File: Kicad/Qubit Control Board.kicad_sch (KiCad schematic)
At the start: 2 parts, among them U1 TRF372017IRGZR, U2 AD9743BCPZ

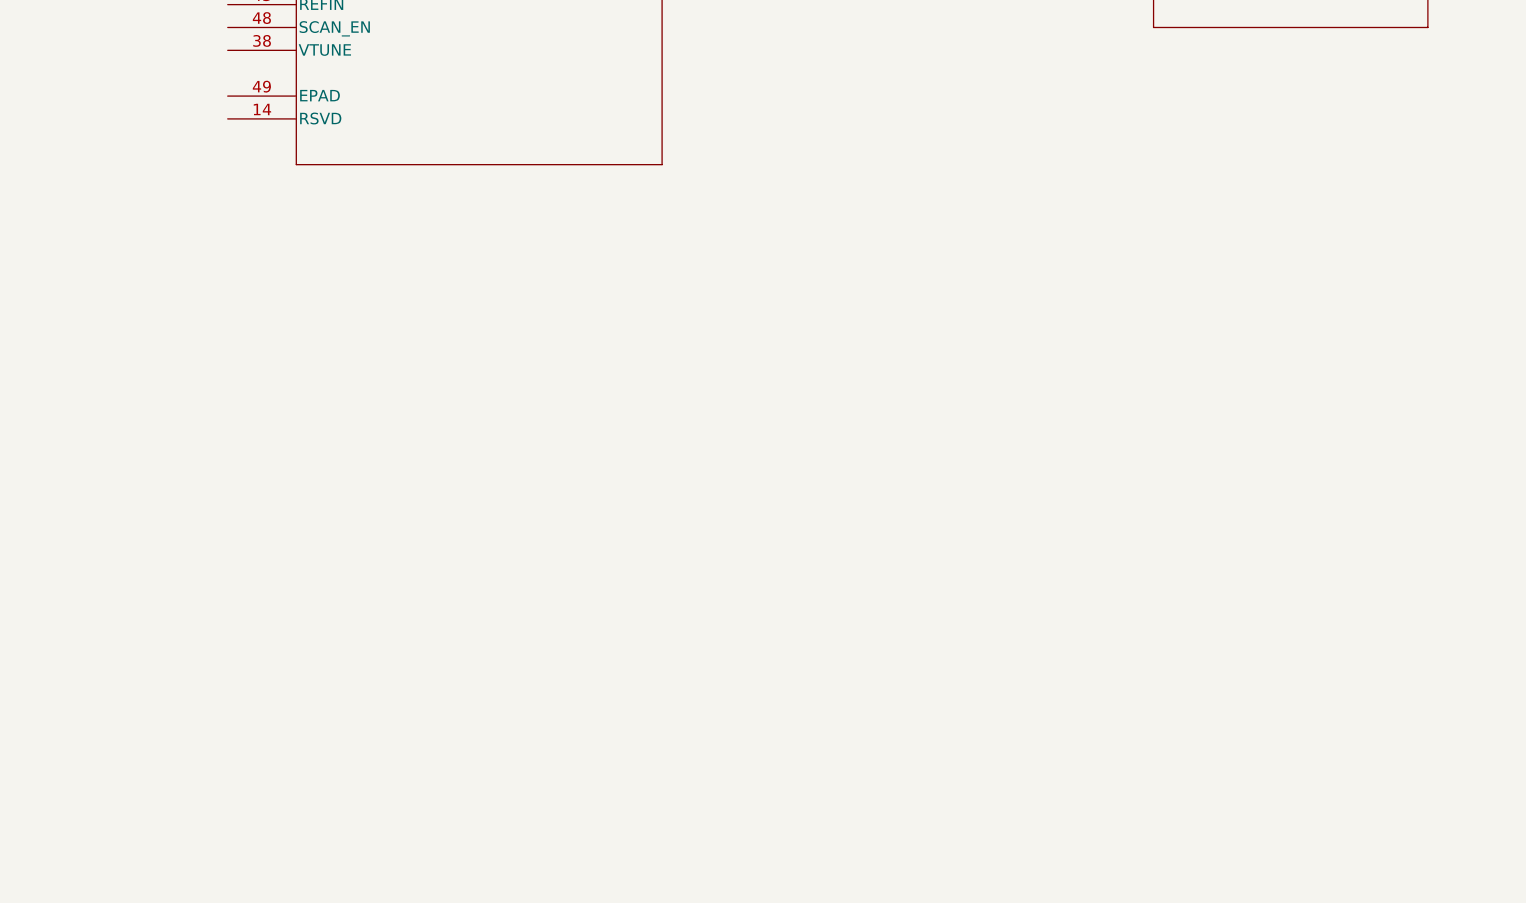
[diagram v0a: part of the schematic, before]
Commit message: Input power set up
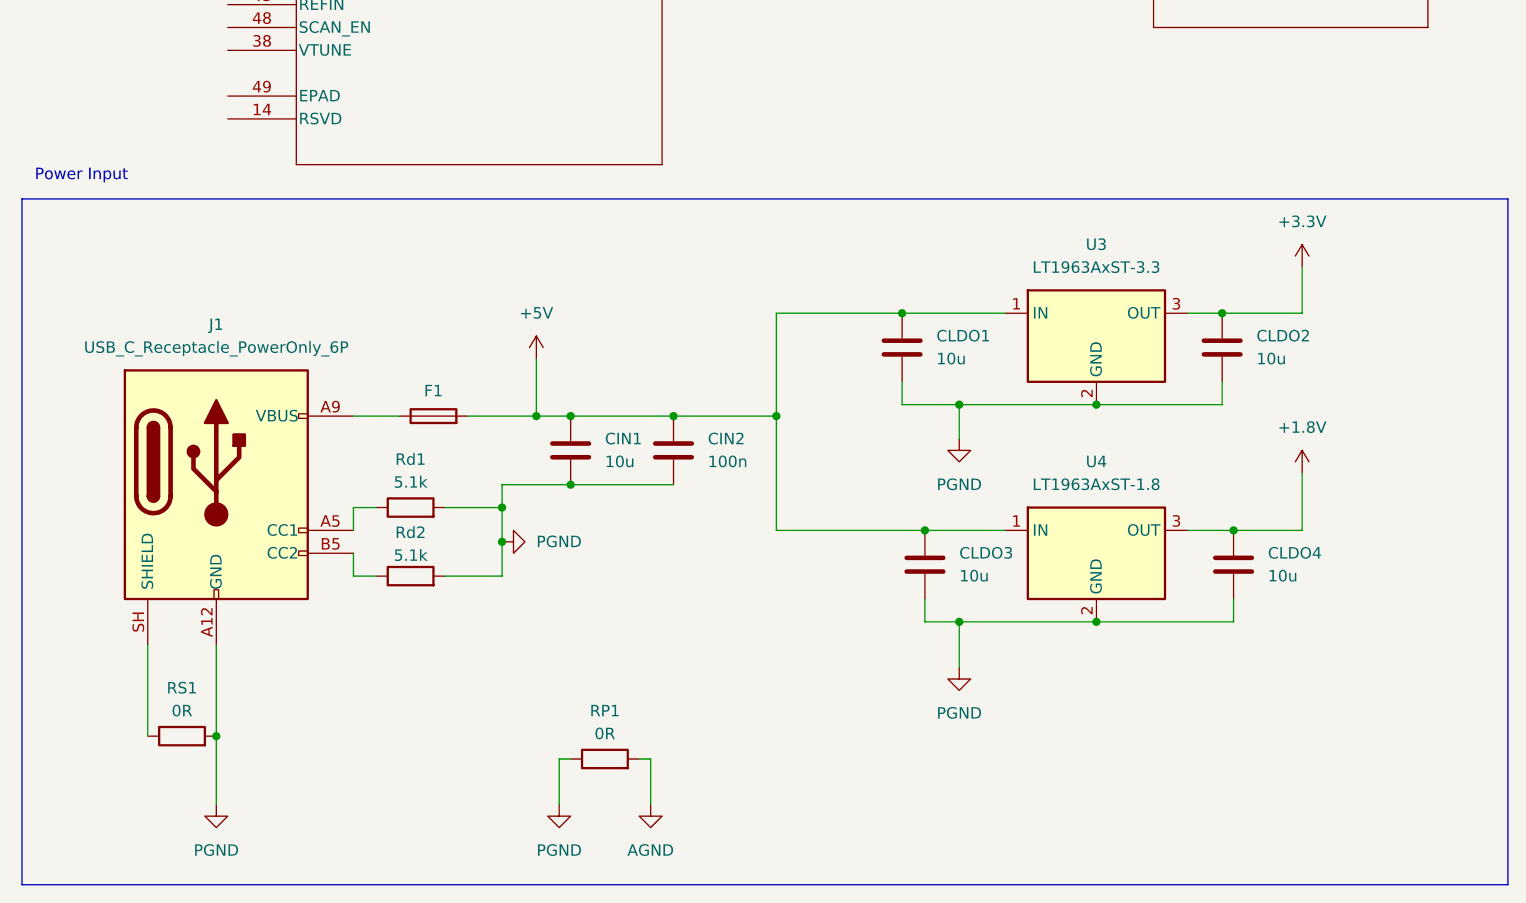
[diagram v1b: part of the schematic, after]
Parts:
- added CIN1, CLDO1, CLDO2, CLDO3, CLDO4: 10u, symbol Device:C
- added CIN2: 100n, symbol Device:C
- added F1: (no value), symbol Device:Fuse
- added J1: USB_C_Receptacle_PowerOnly_6P, symbol Connector:USB_C_Receptacle_PowerOnly_6P
- added RP1, RS1: 0R, symbol Device:R
- added Rd1, Rd2: 5.1k, symbol Device:R
- added U3: LT1963AxST-3.3, Package_TO_SOT_SMD:SOT-223-3_TabPin2, symbol Regulator_Linear:LT1963AxST-3.3
- added U4: LT1963AxST-1.8, Package_TO_SOT_SMD:SOT-223-3_TabPin2, symbol Regulator_Linear:LT1963AxST-1.8
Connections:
- new net: J1.A5 (CC1), Rd1.1
- new net: F1.1, J1.A9 (VBUS), J1.B9 (VBUS)
- new net: J1.B5 (CC2), Rd2.1
- new net: J1.SH (SHIELD), RS1.1
- new net +1.8V: CLDO4.1, U4.3 (OUT)
- new net +3.3V: CLDO2.1, U3.3 (OUT)
- new net +5V: CIN1.1, CIN2.1, CLDO1.1, CLDO3.1, F1.2, U3.1 (IN), U4.1 (IN)
- new net AGND: RP1.2
- new net PGND: CIN1.2, CIN2.2, CLDO1.2, CLDO2.2, CLDO3.2, CLDO4.2, J1.A12 (GND), J1.B12 (GND), RP1.1, RS1.2, Rd1.2, Rd2.2, U3.2 (GND), U4.2 (GND)
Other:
- note added: "Power Input"
- title: (none) -> Qubit Control Board

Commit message: Added DAC
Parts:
- removed RP1: 0R, symbol Device:R
- removed U2: AD9743BCPZ, CP-72-1_ADI, symbol AD9743:AD9743BCPZ
- added CBULK1, CBULK3: 10u, symbol Device:C
- added CBULK2, CBULK4: 1u, symbol Device:C
- added CD1, CD2, CD3, CD4, CD5, CD6, CD7, CD8, CD9, CDC1, CRE1: 100n, symbol Device:C
- added J2: CLK_Pins, symbol Connector_Generic_MountingPin:Conn_01x02_MountingPin
- added J3: Idata, symbol Connector_Generic_MountingPin:Conn_01x11_MountingPin
- added J4: Qdata, symbol Connector_Generic_MountingPin:Conn_01x11_MountingPin
- added RDIFF1: 100R, symbol Device:R
- added RFS1: 10k, symbol Device:R
- added RID0, RID1, RID2, RID3, RID4, RID5, RID6, RID7, RID8, RID9, RQD0, RQD1, RQD2, RQD3, RQD4, RQD5, RQD6, RQD7, RQD8, RQD9, RT1: 33R, symbol Device:R
- added U5: SN65LVDS1DBV, Package_TO_SOT_SMD:SOT-23-5, symbol Interface:SN65LVDS1DBV
- added U6: AD9743BCPZ, CP-72-1_ADI, symbol AD9743BCPZ:AD9743BCPZ
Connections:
- net +1.8V: now also CBULK1.1, CBULK2.1, CD1.2, CD2.2, CD3.2, CD5.1, U6.1 (CVDD18), U6.47 (DVDD18), U6.6 (CVDD18), U6.8 (DVDD18)
- net +3.3V: now also CBULK3.1, CBULK4.1, CD4.2, CD6.2, CD7.2, CD8.2, CD9.2, CDC1.1, U5.1 (V_{CC}), U6.27 (DVDD33), U6.50 (SDIO), U6.53 (RESET), U6.56 (AVDD33), U6.57 (AVDD33), U6.71 (AVDD33), U6.72 (AVDD33)
- net PGND renamed GND
- net GND: now also CBULK1.2, CBULK2.2, CBULK3.2, CBULK4.2, CD1.1, CD2.1, CD3.1, CD4.1, CD5.2, CD6.1, CD7.1, CD8.1, CD9.1, CDC1.2, CRE1.1, J2.1 (Pin_1), J3.1 (Pin_1), J4.1 (Pin_1), RFS1.2, U5.2 (GND), U6.2 (CVSS), U6.28 (DVSS), U6.29 (IQSEL), U6.48 (DVSS), U6.49 (SDO), U6.5 (CVSS), U6.51 (SCLK), U6.52 (CSB), U6.58 (AVSS), U6.61 (AVSS), U6.64 (AVSS), U6.67 (AVSS), U6.7 (DVSS), U6.70 (AVSS), U6.73 (EP)
- new net: J4.5 (Pin_5), RQD3.2
- new net: J4.3 (Pin_3), RQD1.2
- new net: J4.10 (Pin_10), RQD8.2
- new net: J4.11 (Pin_11), RQD9.2
- new net: J4.2 (Pin_2), RQD0.2
- new net: J4.4 (Pin_4), RQD2.2
- new net: J4.6 (Pin_6), RQD4.2
- new net: J4.7 (Pin_7), RQD5.2
- new net: J4.8 (Pin_8), RQD6.2
- new net: J4.9 (Pin_9), RQD7.2
- new net: J3.4 (Pin_4), RID2.2
- new net: J3.7 (Pin_7), RID5.2
- new net: RFS1.1, U6.54 (FSADJ)
- new net: J3.5 (Pin_5), RID3.2
- new net: J3.9 (Pin_9), RID7.2
- new net: J3.10 (Pin_10), RID8.2
- new net: J3.11 (Pin_11), RID9.2
- new net: J3.2 (Pin_2), RID0.2
- new net: J3.3 (Pin_3), RID1.2
- new net: J3.6 (Pin_6), RID4.2
- new net: J3.8 (Pin_8), RID6.2
- new net: J2.2 (Pin_2), RT1.1
- new net: CRE1.2, U6.55 (REFIO)
- new net: RT1.2, U5.5 (D)
- new net CLKN: RDIFF1.2, U5.3 (Z), U6.4 (CLKN)
- new net CLKP: RDIFF1.1, U5.4 (Y), U6.3 (CLKP)
- new net ID0: RID0.1, U6.18 (P1D0)
- new net ID1: RID1.1, U6.17 (P1D1)
- new net ID2: RID2.1, U6.16 (P1D2)
- new net ID3: RID3.1, U6.15 (P1D3)
- new net ID4: RID4.1, U6.14 (P1D4)
- new net ID5: RID5.1, U6.13 (P1D5)
- new net ID6: RID6.1, U6.12 (P1D6)
- new net ID7: RID7.1, U6.11 (P1D7)
- new net ID8: RID8.1, U6.10 (P1D8)
- new net ID9: RID9.1, U6.9 (P1D9)
- new net QD0: RQD0.1, U6.40 (P2D0)
- new net QD1: RQD1.1, U6.39 (P2D1)
- new net QD2: RQD2.1, U6.38 (P2D2)
- new net QD3: RQD3.1, U6.37 (P2D3)
- new net QD4: RQD4.1, U6.36 (P2D4)
- new net QD5: RQD5.1, U6.35 (P2D5)
- new net QD6: RQD6.1, U6.34 (P2D6)
- new net QD7: RQD7.1, U6.33 (P2D7)
- new net QD8: RQD8.1, U6.32 (P2D8)
- new net QD9: RQD9.1, U6.31 (P2D9)
- no-connect marks 0 -> 19
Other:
- moved on the sheet: CIN1, CIN2, CLDO1, CLDO2, CLDO3, CLDO4, F1, J1, RS1, Rd1, Rd2, U1A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

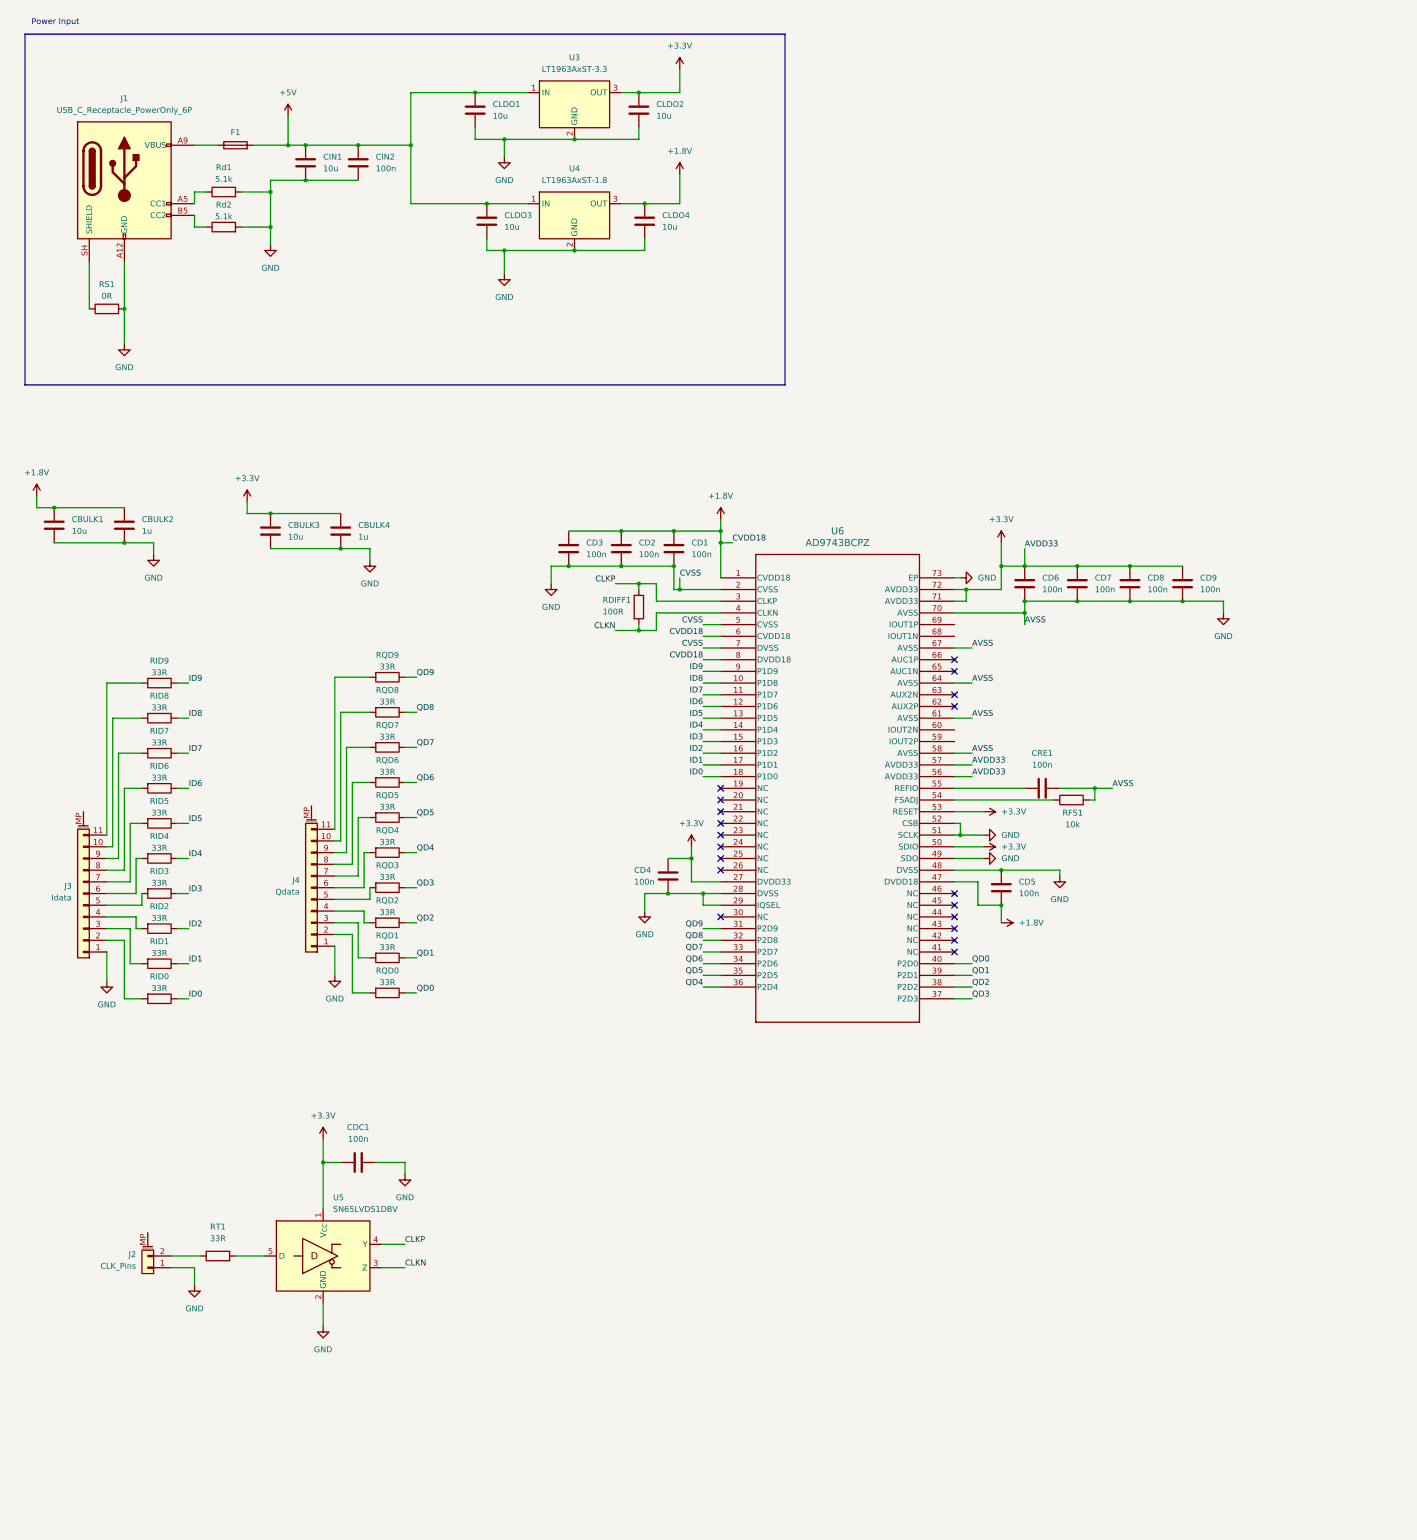
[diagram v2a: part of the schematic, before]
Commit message: Added DAC filtering
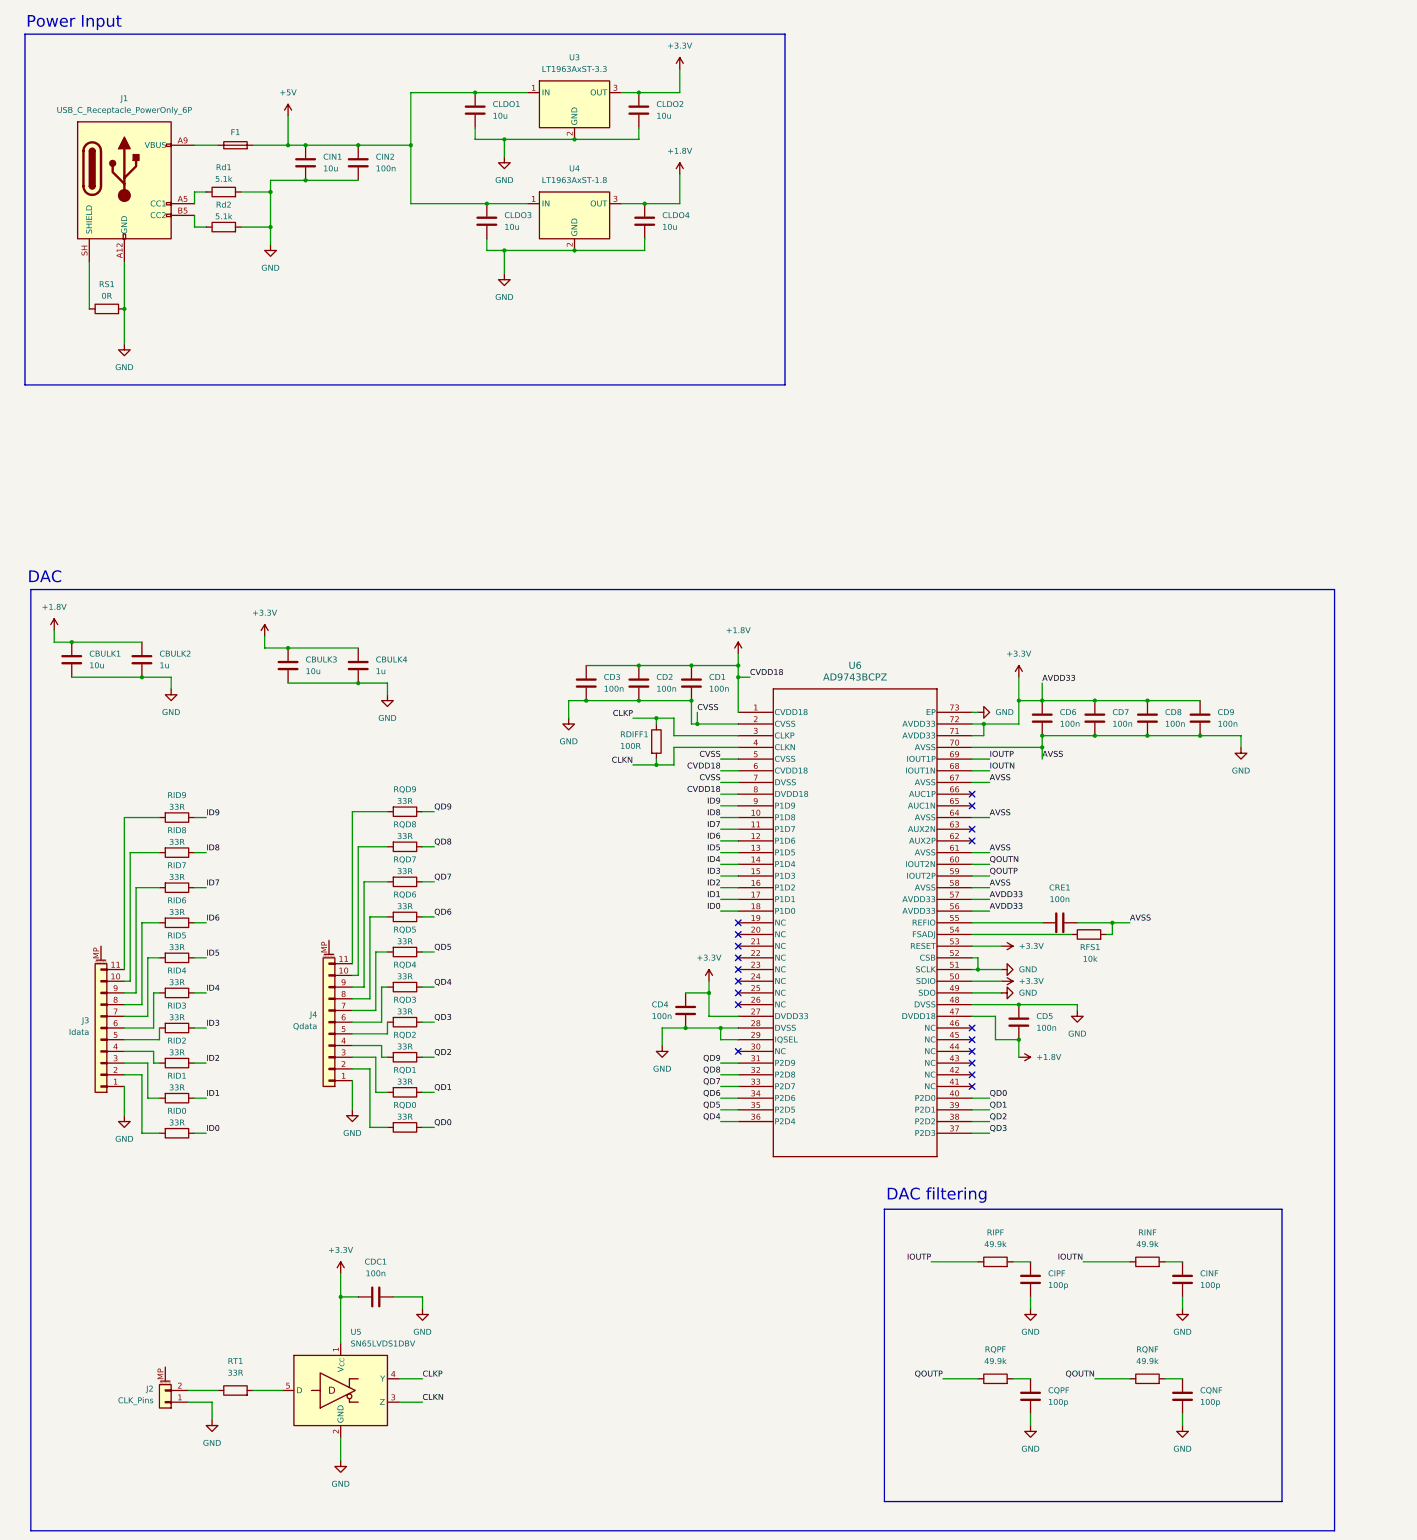
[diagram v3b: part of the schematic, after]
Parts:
- added CINF, CIPF, CQNF, CQPF: 100p, symbol Device:C
- added RINF, RIPF, RQNF, RQPF: 49.9k, symbol Device:R
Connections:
- net GND: now also CINF.2, CIPF.2, CQNF.2, CQPF.2
- net QOUTP: now reaches U6.59 (IOUT2P)
- net QOUTP: now also RQPF.1
- net QOUTN: now reaches U6.60 (IOUT2N)
- net QOUTN: now also RQNF.1
- net IOUTN: now reaches U6.68 (IOUT1N)
- net IOUTN: now also RINF.1
- net IOUTP: now reaches U6.69 (IOUT1P)
- net IOUTP: now also RIPF.1
- new net: CINF.1, RINF.2
- new net: CQNF.1, RQNF.2
- new net: CIPF.1, RIPF.2
- new net: CQPF.1, RQPF.2
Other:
- note added: "DAC"
- note added: "DAC filtering"
- moved on the sheet: CBULK1, CBULK2, CBULK3, CBULK4, CD1, CD2, CD3, CD4, CD5, CD6, CD7, CD8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
